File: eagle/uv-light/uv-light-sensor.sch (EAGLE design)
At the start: 4 parts, among them IC100 SI1147

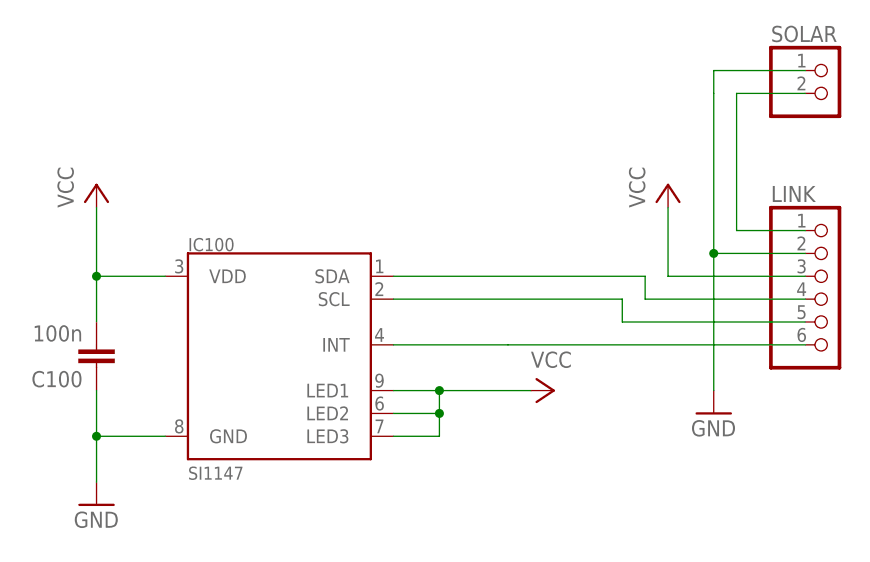
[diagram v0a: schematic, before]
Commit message: CHG: Replaced Si1147 through Si1133
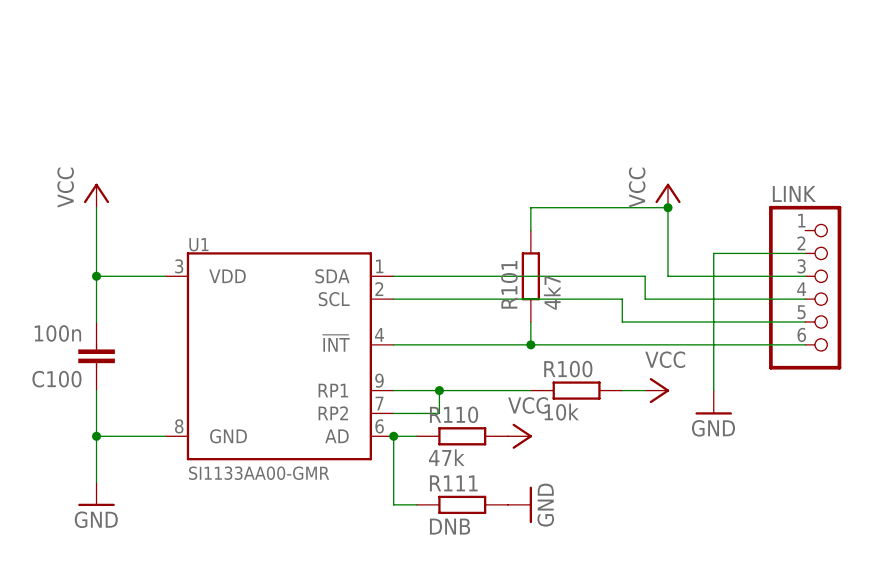
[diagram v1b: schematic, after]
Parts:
- removed IC100: SI1147, weather_station:SI1147
- removed SOLAR: (no value), pinhead:PINHD-1X2
- added R100: 10k, rcl:R-EU_R0603
- added R101: 4k7, rcl:R-EU_R0603
- added R110: 47k, rcl:R-EU_R0603
- added R111: DNB, rcl:R-EU_R0603
- added U1: SI1133AA00-GMR, weather_station:SI1133AA00-GMR
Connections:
- removed net N$4: LINK.1, SOLAR.2
- new net N$5: R100.1, U1.RP1, U1.RP2
- new net N$6: R110.1, R111.1, U1.AD
- net GND: now also R111.2, U1.GND; no longer IC100.GND, SOLAR.1
- net N$1: now also R101.1, U1.!INT; no longer IC100.INT
- net N$2: now also U1.SCL; no longer IC100.SCL
- net N$3: now also U1.SDA; no longer IC100.SDA
- net VCC: now also R100.2, R101.2, R110.2, U1.VDD; no longer IC100.LED1, IC100.LED2, IC100.LED3, IC100.VDD
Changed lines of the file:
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@@
 <?xml version="1.0" encoding="utf-8"?>
 <!DOCTYPE eagle SYSTEM "eagle.dtd">
-<eagle version="6.5.0">
+<eagle version="7.4.0">
 <drawing>
 <settings>
@@
 <layer number="54" name="bGND_GNDA" color="1" fill="9" visible="no" active="no"/>
 <layer number="56" name="wert" color="7" fill="1" visible="no" active="no"/>
+<layer number="90" name="Modules" color="5" fill="1" visible="no" active="yes"/>
 <layer number="91" name="Nets" color="2" fill="1" visible="yes" active="yes"/>
 <layer number="92" name="Busses" color="1" fill="1" visible="yes" active="yes"/>
@@
 <parts>
 <part name="FRAME1" library="frames" deviceset="A4L-LOC" device=""/>
-<part name="IC100" library="weather_station" deviceset="SI1147" device=""/>
 <part name="P+1" library="supply1" deviceset="VCC" device=""/>
 <part name="P+2" library="supply1" deviceset="VCC" device=""/>
@@
 <part name="C100" library="rcl" deviceset="C-EU" device="C0603" value="100n"/>
 <part name="LINK" library="pinhead" deviceset="PINHD-1X6" device=""/>
-<part name="SOLAR" library="pinhead" deviceset="PINHD-1X2" device=""/>
 <part name="P+4" library="supply1" deviceset="VCC" device=""/>
 <part name="GND2" library="supply1" deviceset="GND" device=""/>
+<part name="U1" library="weather_station" deviceset="SI1133" device="AA00-GMR"/>
+<part name="R100" library="rcl" deviceset="R-EU_" device="R0603" value="10k"/>
+<part name="R101" library="rcl" deviceset="R-EU_" device="R0603" value="4k7"/>
+<part name="R110" library="rcl" deviceset="R-EU_" device="R0603" value="47k"/>
+<part name="R111" library="rcl" deviceset="R-EU_" device="R0603" value="DNB"/>
+<part name="GND3" library="supply1" deviceset="GND" device=""/>
+<part name="P+3" library="supply1" deviceset="VCC" device=""/>
 </parts>
 <sheets>
@@
 <instances>
 <instance part="FRAME1" gate="G$1" x="0" y="0"/>
-<instance part="IC100" gate="G$1" x="129.54" y="88.9"/>
 <instance part="P+1" gate="VCC" x="109.22" y="106.68"/>
-<instance part="P+2" gate="VCC" x="160.02" y="83.82" rot="R270"/>
+<instance part="P+2" gate="VCC" x="172.72" y="83.82" rot="R270"/>
 <instance part="GND1" gate="1" x="109.22" y="71.12"/>
 <instance part="C100" gate="G$1" x="109.22" y="86.36" rot="R180"/>
 <instance part="LINK" gate="A" x="190.5" y="93.98"/>
-<instance part="SOLAR" gate="G$1" x="190.5" y="116.84"/>
 <instance part="P+4" gate="VCC" x="172.72" y="106.68"/>
 <instance part="GND2" gate="1" x="177.8" y="81.28"/>
+<instance part="U1" gate="G$1" x="129.54" y="88.9"/>
+<instance part="R100" gate="G$1" x="162.56" y="83.82"/>
+<instance part="R101" gate="G$1" x="157.48" y="96.52" rot="R90"/>
+<instance part="R110" gate="G$1" x="149.86" y="78.74"/>
+<instance part="R111" gate="G$1" x="149.86" y="71.12"/>
+<instance part="GND3" gate="1" x="157.48" y="71.12" rot="R90"/>
+<instance part="P+3" gate="VCC" x="157.48" y="78.74" rot="R270"/>
 </instances>
 <busses>
@@
 <net name="VCC" class="0">
 <segment>
-<pinref part="IC100" gate="G$1" pin="LED1"/>
-<pinref part="P+2" gate="VCC" pin="VCC"/>
-<wire x1="142.24" y1="83.82" x2="147.32" y2="83.82" width="0.1524" layer="91"/>
-<pinref part="IC100" gate="G$1" pin="LED2"/>
-<wire x1="147.32" y1="83.82" x2="157.48" y2="83.82" width="0.1524" layer="91"/>
-<wire x1="142.24" y1="81.28" x2="147.32" y2="81.28" width="0.1524" layer="91"/>
-<wire x1="147.32" y1="81.28" x2="147.32" y2="83.82" width="0.1524" layer="91"/>
-<junction x="147.32" y="83.82"/>
-<pinref part="IC100" gate="G$1" pin="LED3"/>
-<wire x1="142.24" y1="78.74" x2="147.32" y2="78.74" width="0.1524" layer="91"/>
-<wire x1="147.32" y1="78.74" x2="147.32" y2="81.28" width="0.1524" layer="91"/>
-<junction x="147.32" y="81.28"/>
-</segment>
-<segment>
 <pinref part="C100" gate="G$1" pin="2"/>
 <pinref part="P+1" gate="VCC" pin="VCC"/>
 <wire x1="109.22" y1="91.44" x2="109.22" y2="96.52" width="0.1524" layer="91"/>
-<pinref part="IC100" gate="G$1" pin="VDD"/>
 <wire x1="109.22" y1="96.52" x2="109.22" y2="104.14" width="0.1524" layer="91"/>
 <wire x1="116.84" y1="96.52" x2="109.22" y2="96.52" width="0.1524" layer="91"/>
 <junction x="109.22" y="96.52"/>
+<pinref part="U1" gate="G$1" pin="VDD"/>
 </segment>
 <segment>
@@
 <wire x1="172.72" y1="96.52" x2="172.72" y2="104.14" width="0.1524" layer="91"/>
 <pinref part="P+4" gate="VCC" pin="VCC"/>
+<pinref part="R101" gate="G$1" pin="2"/>
+<wire x1="157.48" y1="101.6" x2="157.48" y2="104.14" width="0.1524" layer="91"/>
+<wire x1="157.48" y1="104.14" x2="172.72" y2="104.14" width="0.1524" layer="91"/>
+<junction x="172.72" y="104.14"/>
+</segment>
+<segment>
+<pinref part="P+2" gate="VCC" pin="VCC"/>
+<pinref part="R100" gate="G$1" pin="2"/>
+<wire x1="167.64" y1="83.82" x2="170.18" y2="83.82" width="0.1524" layer="91"/>
+</segment>
+<segment>
+<pinref part="R110" gate="G$1" pin="2"/>
+<pinref part="P+3" gate="VCC" pin="VCC"/>
 </segment>
 </net>
 <net name="GND" class="0">
 <segment>
-<pinref part="IC100" gate="G$1" pin="GND"/>
 <pinref part="GND1" gate="1" pin="GND"/>
 <wire x1="116.84" y1="78.74" x2="109.22" y2="78.74" width="0.1524" layer="91"/>
@@
 <wire x1="109.22" y1="78.74" x2="109.22" y2="83.82" width="0.1524" layer="91"/>
 <junction x="109.22" y="78.74"/>
+<pinref part="U1" gate="G$1" pin="GND"/>
 </segment>
 <segment>
 <pinref part="LINK" gate="A" pin="2"/>
 <wire x1="187.96" y1="99.06" x2="177.8" y2="99.06" width="0.1524" layer="91"/>
-<wire x1="177.8" y1="99.06" x2="177.8" y2="116.84" width="0.1524" layer="91"/>
-<pinref part="SOLAR" gate="G$1" pin="1"/>
-<wire x1="187.96" y1="119.38" x2="177.8" y2="119.38" width="0.1524" layer="91"/>
-<wire x1="177.8" y1="119.38" x2="177.8" y2="116.84" width="0.1524" layer="91"/>
 <wire x1="177.8" y1="99.06" x2="177.8" y2="83.82" width="0.1524" layer="91"/>
-<junction x="177.8" y="99.06"/>
 <pinref part="GND2" gate="1" pin="GND"/>
 </segment>
+<segment>
+<pinref part="R111" gate="G$1" pin="2"/>
+<pinref part="GND3" gate="1" pin="GND"/>
+</segment>
 </net>
 <net name="N$1" class="0">
 <segment>
-<pinref part="IC100" gate="G$1" pin="INT"/>
-<wire x1="142.24" y1="88.9" x2="154.94" y2="88.9" width="0.1524" layer="91"/>
 <pinref part="LINK" gate="A" pin="6"/>
-<wire x1="154.94" y1="88.9" x2="187.96" y2="88.9" width="0.1524" layer="91"/>
+<wire x1="142.24" y1="88.9" x2="157.48" y2="88.9" width="0.1524" layer="91"/>
+<pinref part="U1" gate="G$1" pin="!INT"/>
+<pinref part="R101" gate="G$1" pin="1"/>
+<wire x1="157.48" y1="88.9" x2="187.96" y2="88.9" width="0.1524" layer="91"/>
+<wire x1="157.48" y1="91.44" x2="157.48" y2="88.9" width="0.1524" layer="91"/>
+<junction x="157.48" y="88.9"/>
 </segment>
 </net>
 <net name="N$2" class="0">
 <segment>
-<pinref part="IC100" gate="G$1" pin="SCL"/>
 <wire x1="142.24" y1="93.98" x2="167.64" y2="93.98" width="0.1524" layer="91"/>
 <wire x1="167.64" y1="93.98" x2="167.64" y2="91.44" width="0.1524" layer="91"/>
 <pinref part="LINK" gate="A" pin="5"/>
 <wire x1="167.64" y1="91.44" x2="187.96" y2="91.44" width="0.1524" layer="91"/>
+<pinref part="U1" gate="G$1" pin="SCL"/>
 </segment>
 </net>
 <net name="N$3" class="0">
 <segment>
-<pinref part="IC100" gate="G$1" pin="SDA"/>
 <wire x1="142.24" y1="96.52" x2="170.18" y2="96.52" width="0.1524" layer="91"/>
 <wire x1="170.18" y1="96.52" x2="170.18" y2="93.98" width="0.1524" layer="91"/>
 <pinref part="LINK" gate="A" pin="4"/>
 <wire x1="170.18" y1="93.98" x2="187.96" y2="93.98" width="0.1524" layer="91"/>
-</segment>
-</net>
-<net name="N$4" class="0">
-<segment>
-<pinref part="SOLAR" gate="G$1" pin="2"/>
-<wire x1="187.96" y1="116.84" x2="180.34" y2="116.84" width="0.1524" layer="91"/>
-<wire x1="180.34" y1="116.84" x2="180.34" y2="101.6" width="0.1524" layer="91"/>
-<pinref part="LINK" gate="A" pin="1"/>
-<wire x1="180.34" y1="101.6" x2="187.96" y2="101.6" width="0.1524" layer="91"/>
-</segment>
-</net>
+<pinref part="U1" gate="G$1" pin="SDA"/>
+</segment>
+</net>
+<net name="N$5" class="0">
+<segment>
+<wire x1="142.24" y1="83.82" x2="147.32" y2="83.82" width="0.1524" layer="91"/>
+<wire x1="142.24" y1="81.28" x2="147.32" y2="81.28" width="0.1524" layer="91"/>
+<wire x1="147.32" y1="81.28" x2="147.32" y2="83.82" width="0.1524" layer="91"/>
+<pinref part="U1" gate="G$1" pin="RP1"/>
+<pinref part="U1" gate="G$1" pin="RP2"/>
+<pinref part="R100" gate="G$1" pin="1"/>
+<wire x1="147.32" y1="83.82" x2="157.48" y2="83.82" width="0.1524" layer="91"/>
+<junction x="147.32" y="83.82"/>
+</segment>
+</net>
+<net name="N$6" class="0">
+<segment>
+<pinref part="U1" gate="G$1" pin="AD"/>
+<pinref part="R110" gate="G$1" pin="1"/>
+<wire x1="142.24" y1="78.74" x2="144.78" y2="78.74" width="0.1524" layer="91"/>
+<pinref part="R111" gate="G$1" pin="1"/>
+<wire x1="144.78" y1="71.12" x2="142.24" y2="71.12" width="0.1524" layer="91"/>
+<wire x1="142.24" y1="71.12" x2="142.24" y2="78.74" width="0.1524" layer="91"/>
+<junction x="142.24" y="78.74"/>
+</segment>
+</net>
